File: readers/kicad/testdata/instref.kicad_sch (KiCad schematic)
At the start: 3 parts

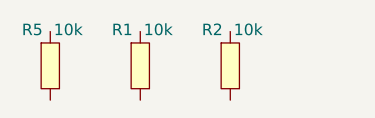
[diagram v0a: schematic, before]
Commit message: readers/kicad: use the shared placeholder-designator predicate
The KiCad reader carried its own `placeholderRef`, matching "?" only as a suffix, while
`internal/refdes.IsPlaceholder` matches it anywhere. A partly-assigned "C?1845" was
therefore a placeholder to one layer and a real designator to the other, which is the
uneven application agni issue 311 names.

This is a behaviour change to board reads, which is why PR 310 left it alone: a footprint
whose reference has a mid-name "?" now gets skipped by the netlist reader, the
board-geometry reader and the silk-text pass, the same way "REF**" already was. On the
schematic side an `instances` entry with such a reference is no longer taken as
post-annotation truth, so the symbol falls back to its property and stays visibly
unannotated instead of acquiring "C?1845" as an identity.

The two fixtures gain the partly-assigned form beside the fully unassigned one they
already carried. Both new assertions were confirmed red with the predicate narrowed back
to a suffix match.
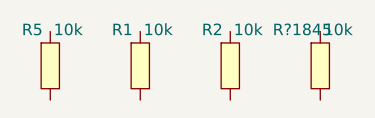
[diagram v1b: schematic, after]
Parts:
- added R?1845: 10k, symbol test:R
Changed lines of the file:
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@@
 					(reference "R7")
+					(unit 1)))))
+	(symbol (lib_id "test:R") (at 80 50 0) (unit 1) (uuid "r-partial")
+		(property "Reference" "R?"
+			(at 78 46 0)
+			(effects (font (size 1.27 1.27))))
+		(property "Value" "10k"
+			(at 82 46 0)
+			(effects (font (size 1.27 1.27))))
+		(instances
+			(project "board"
+				(path "/aaaa-dddd"
+					(reference "R?1845")
 					(unit 1)))))
 	(symbol (lib_id "test:R") (at 70 50 0) (unit 1) (uuid "r-plain")
